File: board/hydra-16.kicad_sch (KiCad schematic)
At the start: 32 parts, among them J1 Conn_01x32, J2 Conn_01x24, J3 DE9_Plug, U3 AT28C64B, U4 W65C02SxP, U5 6522, U6 6551, U7 MAX232, U8 628512_DIP32, U9 74LS154

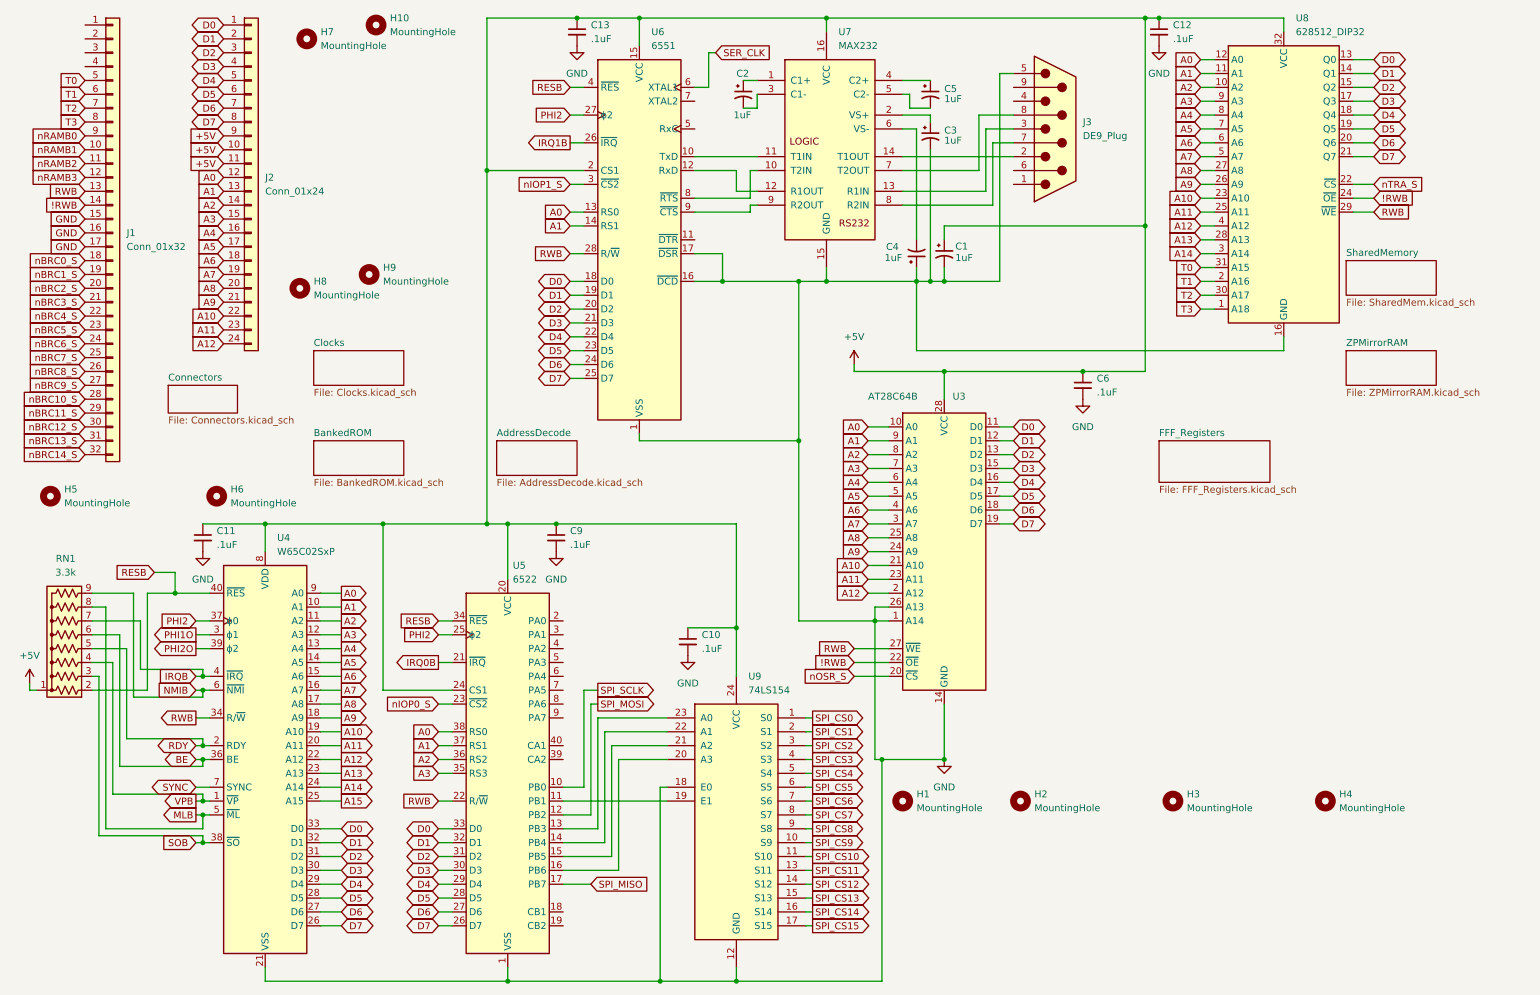
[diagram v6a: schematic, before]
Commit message: More main PCB updates.  Rearranged some things.  Bypass caps near PS connector.  Moved front panel connector to opposite side of board.
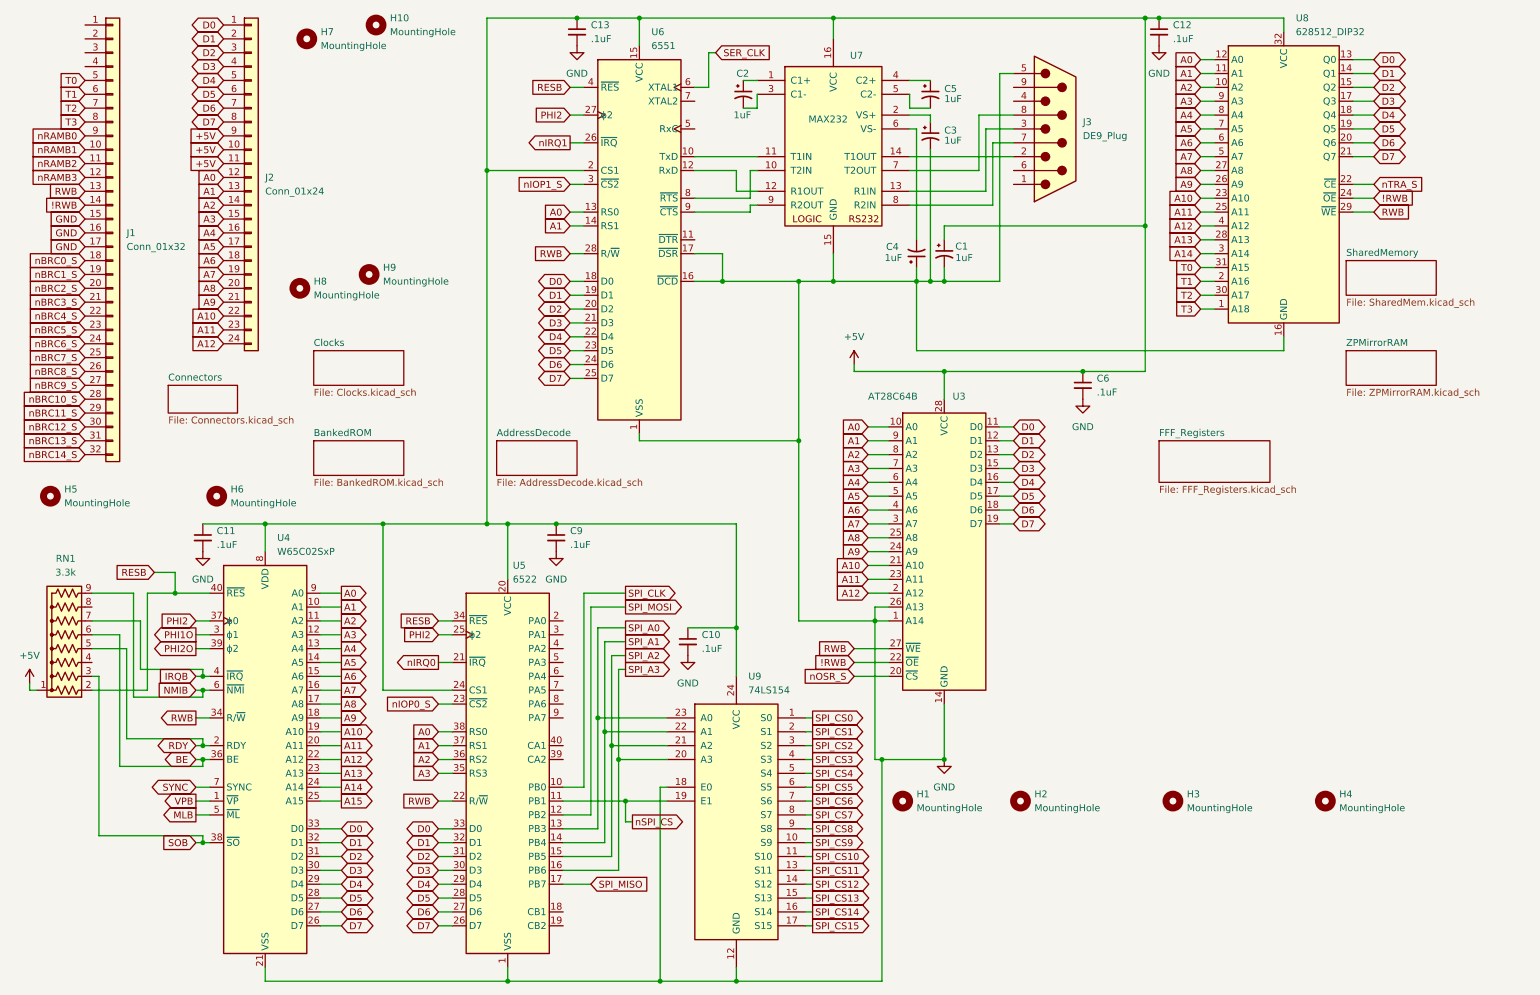
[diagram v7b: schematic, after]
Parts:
- U4, U5: footprint Package_DIP:DIP-40_W15.24mm_Socket_LongPads -> Package_DIP:DIP-40_W15.24mm
- U6: footprint Package_DIP:DIP-28_W15.24mm_Socket_LongPads -> Package_DIP:DIP-28_W15.24mm
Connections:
- net MLB: no longer RN1.8 (R7)
- net VPB: no longer RN1.4 (R3)
- net nSPI_CS: now reaches U5.11 (PB1), U9.19 (E1)
- net SPI_A0: now reaches U5.13 (PB3), U9.23 (A0)
- net SPI_A1: now reaches U5.14 (PB4), U9.22 (A1)
- net SPI_A2: now reaches U5.15 (PB5), U9.21 (A2)
- net SPI_A3: now reaches U5.16 (PB6), U9.20 (A3)
- net IRQ0B renamed nIRQ0
- net IRQ1B renamed nIRQ1
- net SPI_SCLK renamed SPI_CLK
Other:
- moved on the sheet: U7

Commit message: Latest main PCB update with FFF1 and FFF2 added and decode logic updated to exclude FFFE and FFFF in nOSROM_S signal
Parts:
- U4, U5: footprint Package_DIP:DIP-40_W15.24mm -> Package_DIP:DIP-40_W15.24mm_Socket_LongPads
- U6: footprint Package_DIP:DIP-28_W15.24mm -> Package_DIP:DIP-28_W15.24mm_Socket_LongPads
- U7: footprint Package_DIP:DIP-16_W7.62mm_LongPads -> Package_DIP:DIP-16_W7.62mm_Socket_LongPads
- U9: footprint Package_DIP:DIP-24_W15.24mm_LongPads -> Package_DIP:DIP-24_W15.24mm_Socket_LongPads
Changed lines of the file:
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@@
 			)
 		)
-		(property "Footprint" "Package_DIP:DIP-40_W15.24mm"
+		(property "Footprint" "Package_DIP:DIP-40_W15.24mm_Socket_LongPads"
 			(at 104.14 106.68 0)
 			(effects
@@
 			)
 		)
-		(property "Footprint" "Package_DIP:DIP-28_W15.24mm"
+		(property "Footprint" "Package_DIP:DIP-28_W15.24mm_Socket_LongPads"
 			(at 128.27 8.89 0)
 			(effects
@@
 			)
 		)
-		(property "Footprint" "Package_DIP:DIP-16_W7.62mm_LongPads"
+		(property "Footprint" "Package_DIP:DIP-16_W7.62mm_Socket_LongPads"
 			(at 165.1 59.69 0)
 			(effects
@@
 			)
 		)
-		(property "Footprint" "Package_DIP:DIP-24_W15.24mm_LongPads"
+		(property "Footprint" "Package_DIP:DIP-24_W15.24mm_Socket_LongPads"
 			(at 146.05 162.56 0)
 			(effects
@@
 			)
 		)
-		(property "Footprint" "Package_DIP:DIP-40_W15.24mm"
+		(property "Footprint" "Package_DIP:DIP-40_W15.24mm_Socket_LongPads"
 			(at 59.69 101.6 0)
 			(effects
